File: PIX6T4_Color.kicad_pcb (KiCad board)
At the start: 2 copper layers, 88.9 x 33 mm, 179 parts, among them J1 USB_C_Receptacle_USB2.0_16P, J2 Conn_01x18_Pin, J8 Conn_01x03, J9 SM03B-SRSS-TB, SW1 SW_MEC_5G, SW10 SW_MEC_5G, SW11 SW_MEC_5G, SW12 SW_MEC_5G, SW2 SW_MEC_5G, SW3 SW_MEC_5G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

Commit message: Rev. 2
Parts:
- removed G*** (x3): LOGO, LOGO
- added C20: 100nF, Capacitor_SMD:C_0402_1005Metric, F.Cu at (227.5, 106.5)
- added C21: 100nF, Capacitor_SMD:C_0402_1005Metric, F.Cu at (230.5, 106.5)
- added C29: 100nF, Capacitor_SMD:C_0402_1005Metric, F.Cu at (233.5, 106.5)
- added C84: 100nF, Capacitor_SMD:C_0402_1005Metric, F.Cu at (236.5, 106.5)
- added C85: 100nF, Capacitor_SMD:C_0402_1005Metric, F.Cu at (227.5, 109.5)
- added C86: 100nF, Capacitor_SMD:C_0402_1005Metric, F.Cu at (230.5, 109.5)
- added C87: 100nF, Capacitor_SMD:C_0402_1005Metric, F.Cu at (233.5, 109.5)
- added C88: 100nF, Capacitor_SMD:C_0402_1005Metric, F.Cu at (236.5, 109.5)
- added D65: SK6805-EC14, easyeda2kicad:LED-SMD_4P-L1.4-W1.4-TL, F.Cu at (227.5, 105.0)
- added D66: SK6805-EC14, easyeda2kicad:LED-SMD_4P-L1.4-W1.4-TL, F.Cu at (230.5, 105.0)
- added D67: SK6805-EC14, easyeda2kicad:LED-SMD_4P-L1.4-W1.4-TL, F.Cu at (233.5, 105.0)
- added D68: SK6805-EC14, easyeda2kicad:LED-SMD_4P-L1.4-W1.4-TL, F.Cu at (236.5, 105.0)
- added D69: SK6805-EC14, easyeda2kicad:LED-SMD_4P-L1.4-W1.4-TL, F.Cu at (227.5, 108.0)
- added D70: SK6805-EC14, easyeda2kicad:LED-SMD_4P-L1.4-W1.4-TL, F.Cu at (230.5, 108.0)
- added D71: SK6805-EC14, easyeda2kicad:LED-SMD_4P-L1.4-W1.4-TL, F.Cu at (233.5, 108.0)
- added D72: SK6805-EC14, easyeda2kicad:LED-SMD_4P-L1.4-W1.4-TL, F.Cu at (236.5, 108.0)
- moved J8 17.2 mm to (219.7, 113.9), turned to 90 degrees
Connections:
- D64 pad 2: /RGB63/RGB_OUT -> MATRIX_OUT
- J8 pad 2: /RGB63/RGB_OUT -> /RGB71/RGB_OUT
- SW7 pad 3: B -> A
- SW7 pad 4: B -> A
- SW8 pad 3: A -> B
- SW8 pad 4: A -> B
- U3 pad 7: B -> A
- U3 pad 9: A -> B
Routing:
- net GND: track 647.1 -> 716.4 mm, vias 60 -> 68
- net /RGB63/RGB_OUT: track 44.1 -> 0.00 mm, vias 2 -> 0
- net MATRIX_OUT: track 0.00 -> 39.7 mm, vias 0 -> 2
- net +5V: track 385.7 -> 417.4 mm, vias 65 -> 73
- net /RGB71/RGB_OUT: track 0.00 -> 20.0 mm, vias 0 -> 2
- net /RGB67/RGB_OUT: track 0.00 -> 18.1 mm
- net +3V3: track 142.3 -> 154.5 mm
- net B: track 65.7 -> 72.3 mm
- net A: track 72.3 -> 65.7 mm
- net Net-(U3-RUN): track 71.4 -> 68.0 mm
- net Net-(R4-Pad2): track 8.66 -> 5.26 mm
- net /RGB70/RGB_OUT: track 0.00 -> 2.47 mm
- net /RGB69/RGB_OUT: track 0.00 -> 2.47 mm
- net /RGB68/RGB_OUT: track 0.00 -> 2.47 mm
- net /RGB66/RGB_OUT: track 0.00 -> 2.47 mm
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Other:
- board text added: "PIX6T4 Color Rev. 2 © Bertrand Le Roy 2025"
- board text removed: "Contact me at: alice.leroy@digipen.edu"
- board text removed: "PIX6T4 Color (c) Bertrand Le Roy 2025"

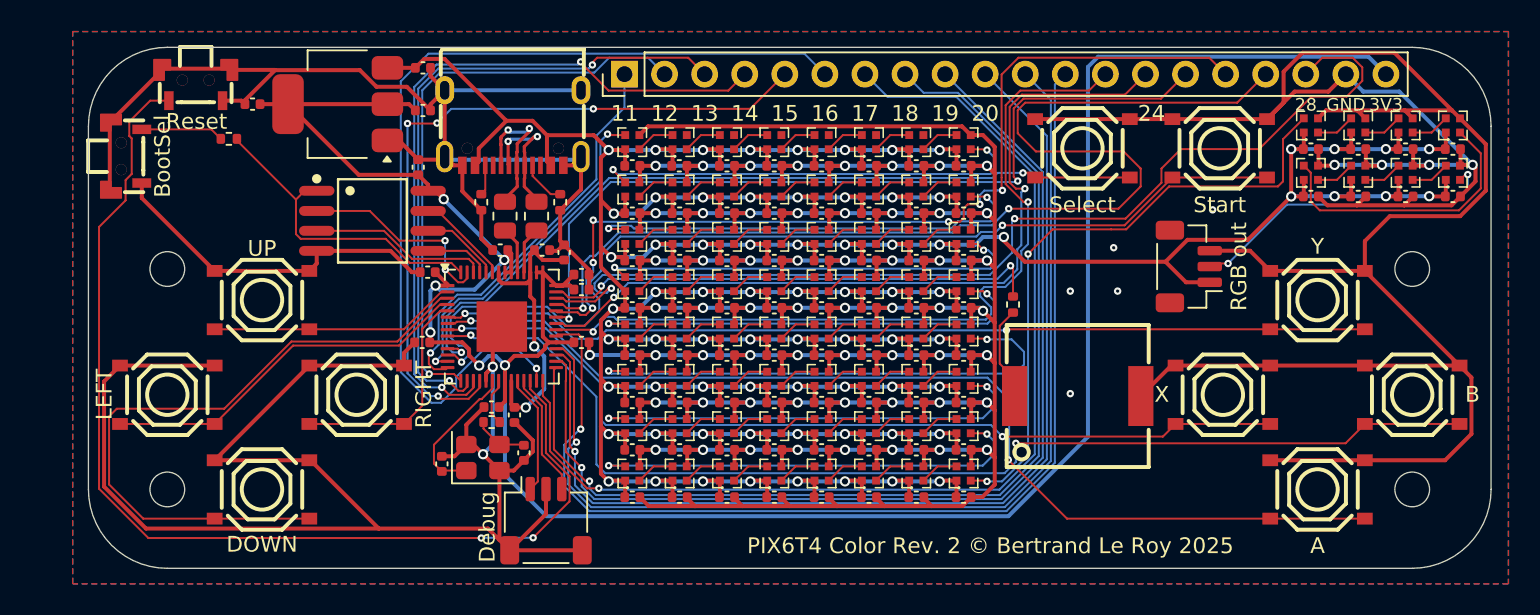
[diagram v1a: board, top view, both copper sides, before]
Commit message: Add power / invader logo light
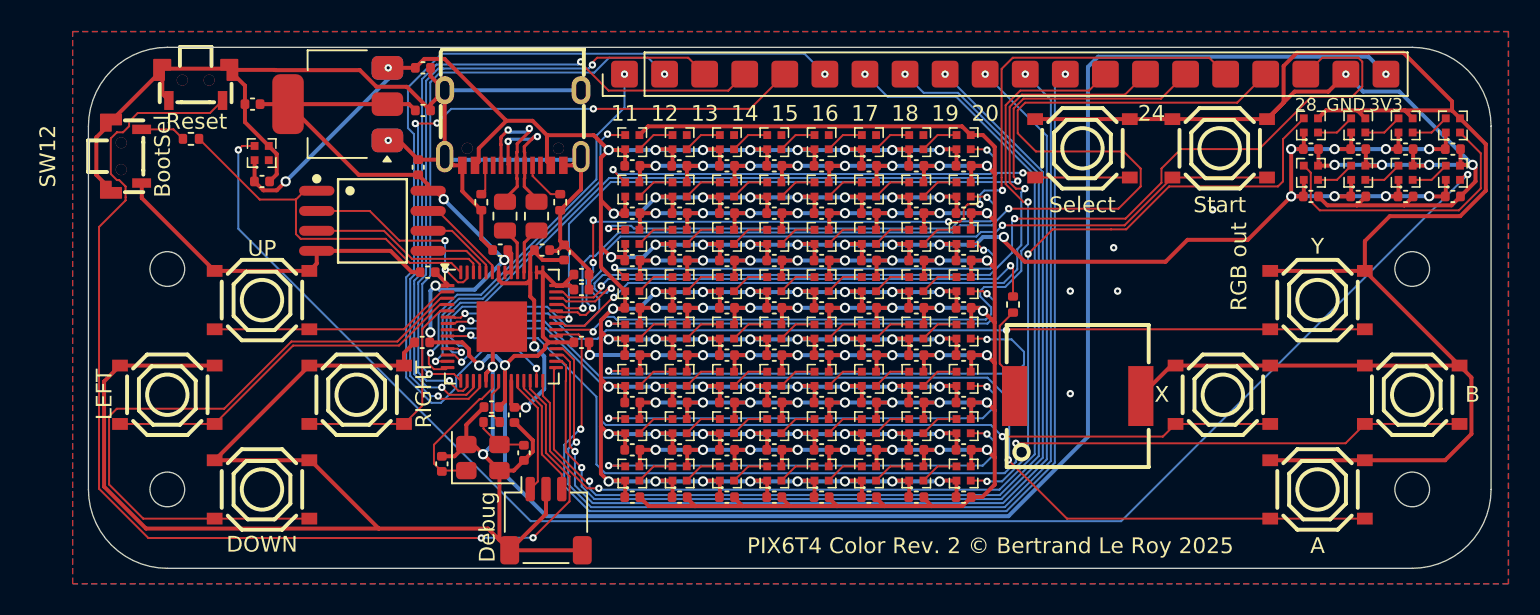
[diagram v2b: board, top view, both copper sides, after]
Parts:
- removed J8: Conn_01x03, Connector_JST:JST_SH_BM03B-SRSS-TB_1x03-1MP_P1.00mm_Vertical
- added C89: 100nF, Capacitor_SMD:C_0402_1005Metric, F.Cu at (161.0, 108.5)
- added D73: SK6805-EC14, easyeda2kicad:LED-SMD_4P-L1.4-W1.4-TL, F.Cu at (161.0, 106.7)
- SW11, SW12: footprint easyeda2kicad:SW-SMD_TS24CA -> easyeda2kicad:SW-SMD_2P-TS24CA
- moved R4 2.40 mm to (156.5, 105.8)
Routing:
- net /RGB71/RGB_OUT: track 20.0 -> 101.5 mm
- net +5V: track 417.4 -> 427.8 mm, vias 73 -> 75
- net Net-(U3-RUN): track 68.0 -> 72.4 mm
- net GND: track 716.4 -> 719.4 mm, vias 68 -> 70
- net Net-(R4-Pad2): track 5.26 -> 2.87 mm
- net Net-(U2-~{CS}): track 20.6 -> 22.9 mm
- net Net-(J2-Pin_6): track 59.0 -> 58.5 mm, vias 1 -> 2
- net Net-(J2-Pin_9): vias 1 -> 2
- net Net-(J2-Pin_8): vias 1 -> 2
- net Net-(J2-Pin_7): vias 1 -> 2
- net Net-(J2-Pin_2): vias 1 -> 2
- net Net-(J2-Pin_12): vias 1 -> 2
- net Net-(J2-Pin_11): vias 1 -> 2
- net Net-(J2-Pin_10): vias 1 -> 2
- net Net-(J2-Pin_1): vias 1 -> 2
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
